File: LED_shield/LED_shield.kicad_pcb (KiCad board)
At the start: 4 copper layers, 80 x 80 mm, 160 parts, among them J101 Screw_Terminal_01x03, J102 Screw_Terminal_01x03, J103 Screw_Terminal_01x03, J104 Screw_Terminal_01x03, J105 Screw_Terminal_01x03, J106 Screw_Terminal_01x03, J107 XLR3, J108 XLR3, J201 Raspberry_Pi_2_3, J301 Screw_Terminal_01x02, Q201 PMOS, Q202 NMOS, Q203 NMOS, Q204 NMOS, Q205 NMOS, Q301 NMOS, Q302 NMOS, Q303 NMOS, Q304 NMOS, Q305 NMOS, SW201 SW_DIP_x08, SW202 SW_DIP_x08, U201 7414, U202 7414, U203 4052, U301 LM25149RGYR, U302 LM25149RGYR, U303 LM74700, U401 SP3485EN, U402 SP3485EN

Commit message: Finish most of PCB design
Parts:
- removed A201: Arduino_Nano_ESP32_Socket, PCM_arduino-library:Arduino_Nano_ESP32_Socket
- removed C202, C403, C404: 100n, Capacitor_SMD:C_0402_1005Metric
- removed C401, C402: 220p, Capacitor_SMD:C_0603_1608Metric
- removed J201: Raspberry_Pi_2_3, Connector_PinSocket_2.54mm:PinSocket_2x17_P2.54mm_Vertical
- removed R201: 1k, Resistor_SMD:R_0603_1608Metric
- removed the R211 at (173.3, 35.6)
- removed the R212 at (173.3, 38.1)
- removed R215, R216, R217, R218, R219, R220, R221, R222, R223, R224, R225, R226, R227, R228, R229, R230, R231, R232, R233, R234, R235, R236: 0R, Resistor_SMD:R_0402_1005Metric
- removed the R310 at (77.0, 41.2)
- removed the R311 at (77.0, 37.0)
- removed R401, R404, R405, R408: 523R, Capacitor_SMD:C_0603_1608Metric
- removed R402, R403, R406, R407: 60R, Resistor_SMD:R_0603_1608Metric
- removed the U203 at (142.6, 103.9)
- removed U401, U402: SP3485EN, Package_SO:SOIC-8_3.9x4.9mm_P1.27mm
- added C204: 100n, Capacitor_SMD:C_0402_1005Metric, F.Cu at (96.5, 103.5)
- added C205: 100n, Capacitor_SMD:C_0402_1005Metric, F.Cu at (112.5, 50.5)
- added J103: Screw_Terminal_01x02, Connector_Phoenix_MC:PhoenixContact_MCV_1,5_2-G-3.81_1x02_P3.81mm_Vertical, B.Cu at (105.0, 43.2)
- added J104: Screw_Terminal_01x02, Connector_Phoenix_MC:PhoenixContact_MCV_1,5_2-G-3.81_1x02_P3.81mm_Vertical, B.Cu at (95.0, 43.2)
- added J106: Screw_Terminal_01x02, Connector_Phoenix_MC:PhoenixContact_MCV_1,5_2-G-3.81_1x02_P3.81mm_Vertical, B.Cu at (55.0, 55.0)
- added J112: Screw_Terminal_01x03, Connector_PinHeader_2.00mm:PinHeader_1x03_P2.00mm_Vertical, B.Cu at (122.5, 108.5)
- added NT301: NetTie_2, NetTie:NetTie-2_SMD_Pad2.0mm, F.Cu at (74.0, 41.0)
- J105: value Screw_Terminal_01x03 -> Screw_Terminal_01x02; footprint Connector_Phoenix_MC:PhoenixContact_MCV_1,5_3-G-3.81_1x03_P3.81mm_Vertical -> Connector_Phoenix_MC:PhoenixContact_MCV_1,5_2-G-3.81_1x02_P3.81mm_Vertical
- J107, J108: value XLR3 -> Screw_Terminal_01x02; footprint Connector_Phoenix_MC:PhoenixContact_MCV_1,5_3-G-3.81_1x03_P3.81mm_Vertical -> Connector_Phoenix_MC:PhoenixContact_MCV_1,5_2-G-3.81_1x02_P3.81mm_Vertical; moved to B.Cu
- J109: renamed from J102; footprint Connector_Phoenix_MC:PhoenixContact_MCV_1,5_3-G-3.81_1x03_P3.81mm_Vertical -> Connector_PinHeader_2.00mm:PinHeader_1x03_P2.00mm_Vertical; moved to B.Cu
- J110: renamed from J103; footprint Connector_Phoenix_MC:PhoenixContact_MCV_1,5_3-G-3.81_1x03_P3.81mm_Vertical -> Connector_PinHeader_2.00mm:PinHeader_1x03_P2.00mm_Vertical
- J111: renamed from J104; footprint Connector_Phoenix_MC:PhoenixContact_MCV_1,5_3-G-3.81_1x03_P3.81mm_Vertical -> Connector_PinHeader_2.00mm:PinHeader_1x03_P2.00mm_Vertical
- J113: renamed from J101; footprint Connector_Phoenix_MC:PhoenixContact_MCV_1,5_3-G-3.81_1x03_P3.81mm_Vertical -> Connector_PinHeader_2.00mm:PinHeader_1x03_P2.00mm_Vertical
- J114: renamed from J106; footprint Connector_Phoenix_MC:PhoenixContact_MCV_1,5_3-G-3.81_1x03_P3.81mm_Vertical -> Connector_PinHeader_2.00mm:PinHeader_1x03_P2.00mm_Vertical
- R202, R203: footprint Resistor_SMD:R_0603_1608Metric -> Resistor_SMD:R_0402_1005Metric
- R205: renamed from R210; footprint Resistor_SMD:R_0603_1608Metric -> Resistor_SMD:R_0402_1005Metric
- R209: renamed from R213; footprint Resistor_SMD:R_0603_1608Metric -> Resistor_SMD:R_0402_1005Metric
- R210: renamed from R214; footprint Resistor_SMD:R_0603_1608Metric -> Resistor_SMD:R_0402_1005Metric
- R211: renamed from R206; footprint Resistor_SMD:R_0603_1608Metric -> Resistor_SMD:R_0402_1005Metric
- R212: renamed from R205; footprint Resistor_SMD:R_0603_1608Metric -> Resistor_SMD:R_0402_1005Metric
- R213: renamed from R207; footprint Resistor_SMD:R_0603_1608Metric -> Resistor_SMD:R_0402_1005Metric
- R214: renamed from R208; footprint Resistor_SMD:R_0603_1608Metric -> Resistor_SMD:R_0402_1005Metric
- SW201, SW202: moved to F.Cu
- moved SW202 151.2 mm to (108.9, 87.0)
- moved SW201 146.0 mm to (108.9, 77.4), turned to 90 degrees
- moved J110 143.3 mm to (105.4, 37.0), turned to 90 degrees
- moved J111 132.5 mm to (96.4, 37.0), turned to 90 degrees
- moved Q205 104.6 mm to (95.5, 78.5), turned to 180 degrees
- moved R205 102.9 mm to (93.5, 98.0)
- moved Q204 102.0 mm to (95.5, 83.1), turned to 180 degrees
- moved Q203 100.3 mm to (95.5, 87.6), turned to 180 degrees
- moved Q202 99.3 mm to (95.6, 92.1), turned to 180 degrees
- moved C201 97.4 mm to (93.5, 99.0)
- moved Q201 95.9 mm to (104.0, 62.0), turned to 180 degrees
- moved R204 93.8 mm to (91.5, 98.0), turned to -90 degrees
- moved R211 92.0 mm to (96.5, 94.3), turned to 180 degrees
- moved R212 90.8 mm to (96.5, 89.8), turned to 180 degrees
- moved R213 85.4 mm to (96.5, 85.3), turned to 180 degrees
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- renumbered C335 to C301, C337 to C302, C336 to C303, C309 to C304, C301 to C305, C316 to C306, C324 to C307, C302 to C308, C317 to C309, C303 to C310, C318 to C311, C315 to C312, C330 to C313, C304 to C314, C319 to C315, C314 to C316, C329 to C317, C305 to C318, C320 to C319, C306 to C320, C333 to C322, C334 to C323, C307 to C324, C322 to C325, C308 to C326, C323 to C327, C310 to C328, C325 to C329, C311 to C330, C326 to C331, C312 to C332, C327 to C333, C313 to C334, C328 to C335, C331 to C336, C332 to C337, R209 to R204, R204 to R208, R318 to R301, R305 to R302, R306 to R303, R316 to R304, R317 to R305, R307 to R306, R319 to R307, R303 to R308, R314 to R309, R308 to R310, R320 to R311, R309 to R313, R321 to R314, R323 to R315, R324 to R316, R313 to R317, R322 to R318, R304 to R319, R315 to R320, U201 to U203, U303 to U301, U301 to U302, U302 to U303
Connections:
- A202 pad 1: /IO/LED0_MCU -> unconnected-(A202-GPIO0-Pad1)
- A202 pad 10: /IO/btn_sel3 -> /IO/LED3_MCU
- A202 pad 15: /IO/btn_read1 -> /IO/LED2_MCU
- A202 pad 19: /IO/btn_read2 -> /IO/LED1_MCU
- A202 pad 2: /IO/LED1_MCU -> unconnected-(A202-GPIO1-Pad2)
- A202 pad 20: /IO/btn_read3 -> /IO/LED0_MCU
- A202 pad 21: /IO/LED4_MCU -> /IO/btn_read1
- A202 pad 22: /IO/LED5_MCU -> /IO/btn_read3
- A202 pad 24: unconnected-(A202-GPIO18-Pad24) -> /IO/btn_read2
- A202 pad 25: unconnected-(A202-GPIO19-Pad25) -> /IO/btn_sel1
- A202 pad 26: unconnected-(A202-GPIO20-Pad26) -> /IO/btn_sel2
- A202 pad 27: unconnected-(A202-GPIO21-Pad27) -> /IO/btn_sel3
- A202 pad 29: unconnected-(A202-GPIO22-Pad29) -> /IO/btn_sel0
- A202 pad 4: /IO/LED2_MCU -> unconnected-(A202-GPIO2-Pad4)
- A202 pad 5: /IO/LED3_MCU -> unconnected-(A202-GPIO3-Pad5)
- A202 pad 6: /IO/btn_sel0 -> unconnected-(A202-GPIO4-Pad6)
- A202 pad 7: /IO/btn_sel1 -> /IO/LED5_MCU
- A202 pad 9: /IO/btn_sel2 -> /IO/LED4_MCU
- C201 pad 1: Net-(U203-X0) -> /IO/ADC_{0}MCU
- C203 pad 1: Net-(U203-X1) -> /IO/ADC_{1}MCU
- J105 pad 1: /+5V_{b} -> +5V
- J105 pad 2: unconnected-(J105-Pin_2-Pad2) -> GND
- J107 pad 1: unconnected-(J107-Pad1) -> /+5V_{b}
- J107 pad 2: unconnected-(J107-Pad2) -> GND
- J108 pad 1: unconnected-(J108-Pad1) -> /+5V_{b}
- J108 pad 2: unconnected-(J108-Pad2) -> GND
- J109 pad 2: unconnected-(J102-Pin_2-Pad2) -> /IO/LED_OUT_0
- J110 pad 2: unconnected-(J103-Pin_2-Pad2) -> /IO/LED_OUT_1
- J111 pad 2: unconnected-(J104-Pin_2-Pad2) -> /IO/LED_OUT_2
- J113 pad 1: /+5V_{b} -> +5V
- J113 pad 2: unconnected-(J101-Pin_2-Pad2) -> /IO/LED_OUT_4
- J114 pad 1: /+5V_{b} -> +5V
- J114 pad 2: unconnected-(J106-Pin_2-Pad2) -> /IO/LED_OUT_5
- R204 pad 1: /IO/12VIN -> /power/VIN
- R204 pad 2: Net-(U203-X0) -> /IO/ADC_{0}MCU
- R205 pad 1: Net-(U203-X0) -> /IO/ADC_{0}MCU
- R209 pad 2: Net-(U203-X1) -> /IO/ADC_{1}MCU
- R210 pad 1: Net-(U203-X1) -> /IO/ADC_{1}MCU
- U202 pad 1: /IO/LED0_MCU -> /IO/LED2_MCU
- U202 pad 10: /IO/LED_OUT_4 -> /IO/LED_OUT_1
- U202 pad 11: Net-(U201-Pad10) -> Net-(U202-Pad11)
- U202 pad 12: /IO/LED_OUT_5 -> /IO/LED_OUT_2
- U202 pad 13: Net-(U201-Pad12) -> Net-(U202-Pad13)
- U202 pad 2: Net-(U201-Pad1) -> Net-(U202-Pad13)
- U202 pad 4: Net-(U201-Pad3) -> Net-(U202-Pad11)
- U202 pad 5: /IO/LED2_MCU -> /IO/LED0_MCU
- U202 pad 6: Net-(U201-Pad5) -> Net-(U202-Pad6)
- U202 pad 8: Net-(U201-Pad9) -> /IO/LED_OUT_0
- U202 pad 9: /IO/LED3_MCU -> Net-(U202-Pad6)
- U203 pad 1: Net-(U201-Pad1) -> /IO/LED5_MCU
- U203 pad 10: Net-(U201-Pad10) -> /IO/LED_OUT_4
- U203 pad 11: /IO/LED4_MCU -> Net-(U203-Pad11)
- U203 pad 12: Net-(U201-Pad12) -> /IO/LED_OUT_5
- U203 pad 13: /IO/LED5_MCU -> Net-(U203-Pad13)
- U203 pad 2: /IO/LED_OUT_0 -> Net-(U203-Pad13)
- U203 pad 3: Net-(U201-Pad3) -> /IO/LED4_MCU
- U203 pad 4: /IO/LED_OUT_1 -> Net-(U203-Pad11)
- U203 pad 5: Net-(U201-Pad5) -> /IO/LED3_MCU
- U203 pad 6: /IO/LED_OUT_2 -> Net-(U203-Pad6)
- U203 pad 9: Net-(U201-Pad9) -> Net-(U203-Pad6)
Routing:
- net /IO/LED3_MCU: track 0.00 -> 58.0 mm, vias 0 -> 3
- net /IO/LED5_MCU: track 0.00 -> 56.5 mm, vias 0 -> 3
- net /IO/LED4_MCU: track 0.00 -> 53.8 mm, vias 0 -> 3
- net GND: track 8.35 -> 54.3 mm, vias 70 -> 459
- net Net-(D205-A): track 0.00 -> 45.0 mm, vias 0 -> 3
- net /IO/3V3: track 0.00 -> 43.5 mm, vias 0 -> 4
- net /+5V_{b}: track 65.5 -> 27.2 mm
- net Net-(A202-VBUS): track 0.00 -> 37.8 mm, vias 0 -> 1
- net Net-(D204-A): track 0.00 -> 37.5 mm, vias 0 -> 3
- net /IO/5V_local: track 0.00 -> 37.5 mm, vias 0 -> 1
- net +5V: track 66.8 -> 103.7 mm
- net Net-(D203-A): track 0.00 -> 30.9 mm, vias 0 -> 3
- net /IO/ADC_{0}MCU: track 0.00 -> 28.5 mm, vias 0 -> 1
- net /IO/LED_OUT_3: track 0.00 -> 26.8 mm, vias 0 -> 1
- net /IO/ADC_{1}MCU: track 0.00 -> 26.5 mm, vias 0 -> 1
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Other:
- board size 80 x 80 mm -> 79 x 80 mm

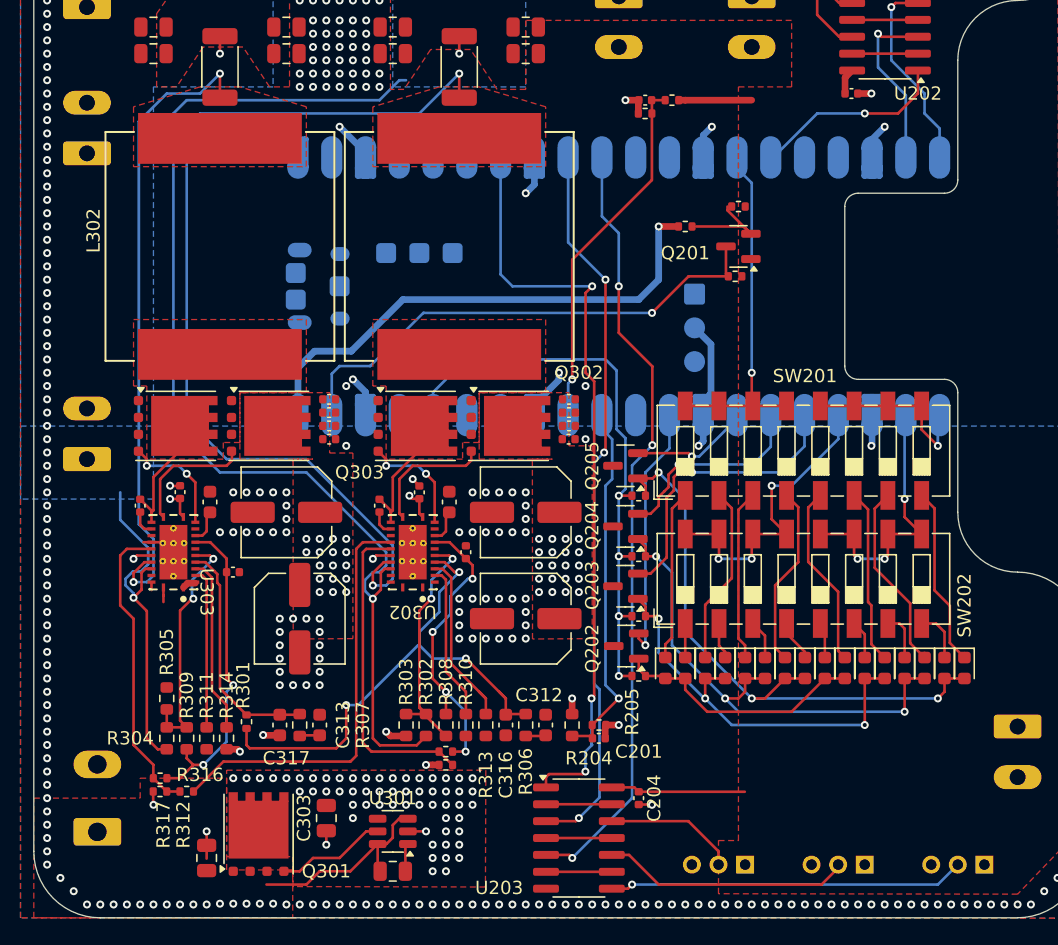
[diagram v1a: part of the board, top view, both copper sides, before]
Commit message: Remove unused components
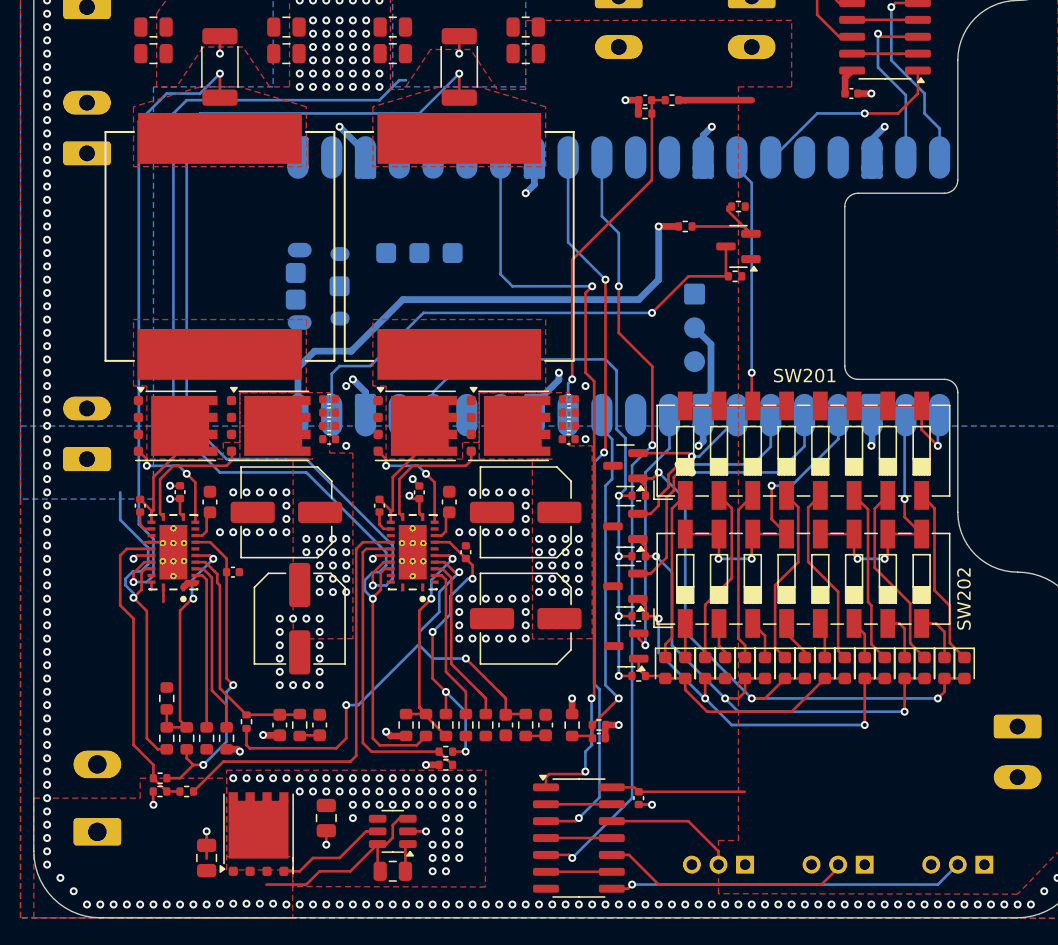
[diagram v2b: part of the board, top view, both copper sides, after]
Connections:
- net /+5V_{b} renamed /power/+5V_{b}
- net /power/VIN renamed /IO/VIN

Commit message: Small fixes before production
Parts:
- removed D202, D203, D204, D205, D206, D207, D208, D209, D210, D211, D212, D213, D214, D215, D216, D217: D_Small_Filled, Diode_SMD:D_0603_1608Metric
- removed Q202, Q203, Q204, Q205: NMOS, Package_TO_SOT_SMD:SOT-23
- added C202: 100n, Capacitor_SMD:C_0402_1005Metric, F.Cu at (122.0, 105.0)
- added C206: 100n, Capacitor_SMD:C_0402_1005Metric, F.Cu at (99.0, 63.5)
- added R201: 100k, Resistor_SMD:R_0402_1005Metric, F.Cu at (120.0, 93.5)
- added R206: 100k, Resistor_SMD:R_0402_1005Metric, F.Cu at (120.0, 96.5)
- added R207: 100k, Resistor_SMD:R_0402_1005Metric, F.Cu at (120.0, 98.0)
- added R215: 100k, Resistor_SMD:R_0402_1005Metric, F.Cu at (100.5, 100.0)
- added R216: 100k, Resistor_SMD:R_0402_1005Metric, F.Cu at (109.5, 70.5)
- added R217: 100k, Resistor_SMD:R_0402_1005Metric, F.Cu at (109.5, 72.5)
- added R218: 100k, Resistor_SMD:R_0402_1005Metric, F.Cu at (103.5, 73.0)
- added R219: 100k, Resistor_SMD:R_0402_1005Metric, F.Cu at (101.0, 73.5)
- added R220: 100k, Resistor_SMD:R_0402_1005Metric, F.Cu at (100.5, 62.0)
- added R221: 100k, Resistor_SMD:R_0402_1005Metric, F.Cu at (101.5, 62.0)
- added R222: 100k, Resistor_SMD:R_0402_1005Metric, F.Cu at (102.5, 62.0)
- added R223: 100k, Resistor_SMD:R_0402_1005Metric, F.Cu at (103.5, 62.0)
- added R321: 82k, Resistor_SMD:R_0603_1608Metric, F.Cu at (84.0, 95.0)
- added U201: 74HC165, Package_SO:SOIC-16_3.9x9.9mm_P1.27mm, F.Cu at (103.5, 68.5)
- added U204: 74HC165, Package_SO:SOIC-16_3.9x9.9mm_P1.27mm, F.Cu at (116.0, 102.5)
- C312, C313: value 4.7nF -> 5.6nF
- C316, C317: value 91pF -> 470pF
- R211, R212, R213, R214: value 10k -> 100k
- R302, R304: footprint Resistor_SMD:R_0603_1608Metric -> Resistor_SMD:R_0402_1005Metric
- R306, R307: value 9k09 -> 5k1
- R310: value 71k5 -> 560k
- R311: value 90k9 -> 91k
- R313, R314: value 71k5 -> 75k
- R319, R320: footprint Resistor_SMD:R_2010_5025Metric -> Resistor_SMD:R_1206_3216Metric
- SW201, SW202: footprint Button_Switch_SMD:SW_DIP_SPSTx08_Slide_6.7x21.88mm_W6.73mm_P2.54mm_LowProfile_JPin -> Button_Switch_SMD:SW_DIP_SPSTx08_Slide_6.7x21.88mm_W8.61mm_P2.54mm_LowProfile
- moved R214 20.0 mm to (102.0, 100.0), turned to -90 degrees
- moved R213 16.5 mm to (104.0, 100.0), turned to -90 degrees
- moved SW201 15.2 mm to (107.5, 92.5)
- moved R212 14.3 mm to (106.5, 100.0), turned to -90 degrees
- moved R211 13.3 mm to (108.5, 100.0), turned to -90 degrees
- moved SW202 7.14 mm to (107.5, 80.0)
- moved Q201 4.54 mm to (103.9, 57.5), turned to 0 degrees
- moved R202 4.54 mm to (99.9, 56.0)
- moved R203 4.54 mm to (103.9, 54.5)
- moved R208 4.54 mm to (103.7, 59.7)
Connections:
- A202 pad 21: /IO/btn_read1 -> /IO/Ser_in
- A202 pad 22: /IO/btn_read3 -> unconnected-(A202-GPIO17-Pad22)
- A202 pad 24: /IO/btn_read2 -> /IO/CP
- A202 pad 25: /IO/btn_sel1 -> /IO/~{PL}
- A202 pad 26: /IO/btn_sel2 -> /IO/~{CE}
- A202 pad 27: /IO/btn_sel3 -> unconnected-(A202-GPIO21-Pad27)
- A202 pad 29: /IO/btn_sel0 -> unconnected-(A202-GPIO22-Pad29)
- Q201 pad 1: +5V -> Net-(Q201-G)
- Q201 pad 2: Net-(Q201-G) -> /IO/5V_local
- Q201 pad 3: /IO/5V_local -> +5V
- R211 pad 1: Net-(D202-A) -> Net-(U204-D4)
- R211 pad 2: /IO/3V3 -> GND
- R212 pad 1: Net-(D203-A) -> Net-(U204-D3)
- R212 pad 2: /IO/3V3 -> GND
- R213 pad 1: Net-(D204-A) -> Net-(U204-D2)
- R213 pad 2: /IO/3V3 -> GND
- R214 pad 1: Net-(D205-A) -> Net-(U204-D1)
- R214 pad 2: /IO/3V3 -> GND
- SW201 pad 10: /IO/btn_read1 -> /IO/3V3
- SW201 pad 11: /IO/btn_read1 -> /IO/3V3
- SW201 pad 12: /IO/btn_read1 -> /IO/3V3
- SW201 pad 13: /IO/btn_read0 -> /IO/3V3
- SW201 pad 14: /IO/btn_read0 -> /IO/3V3
- SW201 pad 15: /IO/btn_read0 -> /IO/3V3
- SW201 pad 16: /IO/btn_read0 -> /IO/3V3
- SW201 pad 2: Net-(D203-K) -> Net-(U204-D1)
- SW201 pad 3: Net-(D204-K) -> Net-(U204-D2)
- SW201 pad 4: Net-(D205-K) -> Net-(U204-D3)
- SW201 pad 5: Net-(D206-K) -> Net-(U204-D4)
- SW201 pad 9: /IO/btn_read1 -> /IO/3V3
- SW202 pad 1: Net-(D210-K) -> /IO/3V3
- SW202 pad 10: /IO/btn_read3 -> Net-(U201-D6)
- SW202 pad 11: /IO/btn_read3 -> Net-(U201-D5)
- SW202 pad 12: /IO/btn_read3 -> Net-(U201-D4)
- SW202 pad 13: /IO/btn_read2 -> Net-(U201-D3)
- SW202 pad 14: /IO/btn_read2 -> Net-(U201-D2)
- SW202 pad 15: /IO/btn_read2 -> Net-(U201-D1)
- SW202 pad 16: /IO/btn_read2 -> Net-(U201-D0)
- SW202 pad 2: Net-(D211-K) -> /IO/3V3
- SW202 pad 3: Net-(D212-K) -> /IO/3V3
- SW202 pad 4: Net-(D213-K) -> /IO/3V3
- SW202 pad 5: Net-(D214-K) -> /IO/3V3
- SW202 pad 6: Net-(D215-K) -> /IO/3V3
- SW202 pad 7: Net-(D216-K) -> /IO/3V3
- SW202 pad 8: Net-(D217-K) -> /IO/3V3
- SW202 pad 9: /IO/btn_read3 -> Net-(U201-D7)
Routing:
- net /IO/3V3: track 43.5 -> 127.4 mm, vias 4 -> 1
- net /IO/~{CE}: track 0.00 -> 67.0 mm, vias 0 -> 4
- net /IO/~{PL}: track 0.00 -> 61.7 mm, vias 0 -> 2
- net /IO/CP: track 0.00 -> 58.7 mm, vias 0 -> 2
- net Net-(U201-DS): track 0.00 -> 55.6 mm, vias 0 -> 4
- net Net-(D205-A): track 45.0 -> 0.00 mm, vias 3 -> 0
- net Net-(D204-A): track 37.5 -> 0.00 mm, vias 3 -> 0
- net Net-(U201-D3): track 0.00 -> 32.4 mm
- net Net-(D203-A): track 30.9 -> 0.00 mm, vias 3 -> 0
- net Net-(U201-D2): track 0.00 -> 29.8 mm
- net Net-(U201-D1): track 0.00 -> 27.6 mm
- net /IO/btn_read0: track 26.0 -> 0.00 mm, vias 1 -> 0
- net /IO/btn_read2: track 24.5 -> 0.00 mm, vias 3 -> 0
- net Net-(U201-D7): track 0.00 -> 23.8 mm, vias 0 -> 3
- net /IO/btn_sel1: track 22.9 -> 0.00 mm, vias 1 -> 0
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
